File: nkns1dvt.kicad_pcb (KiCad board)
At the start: 2 copper layers, 168.9 x 126.5 mm, 79 parts, among them J1 MJ-4PP-9, J2 SERIAL_LED, SW1 SW_RESET, SW10 SW_PUSH, SW11 SW_PUSH, SW12 SW_PUSH, SW13 SW_PUSH, SW14 SW_PUSH, SW15 SW_PUSH, SW16 SW_PUSH, SW17 SW_PUSH, SW18 SW_PUSH, SW19 SW_PUSH, SW2 SW_PUSH, SW20 SW_PUSH, SW21 SW_PUSH, SW22 SW_PUSH, SW23 SW_PUSH, SW24 SW_PUSH, SW25 SW_PUSH, SW26 SW_PUSH, SW27 SW_PUSH, SW28 SW_PUSH, SW29 SW_PUSH, SW3 SW_PUSH, SW30 SW_PUSH, SW31 SW_PUSH, SW32 SW_PUSH, SW33 SW_PUSH, SW34 SW_PUSH, SW4 SW_PUSH, SW5 SW_PUSH, SW6 SW_PUSH, SW7 SW_PUSH, SW8 SW_PUSH, SW9 SW_PUSH, U1 ProMicro

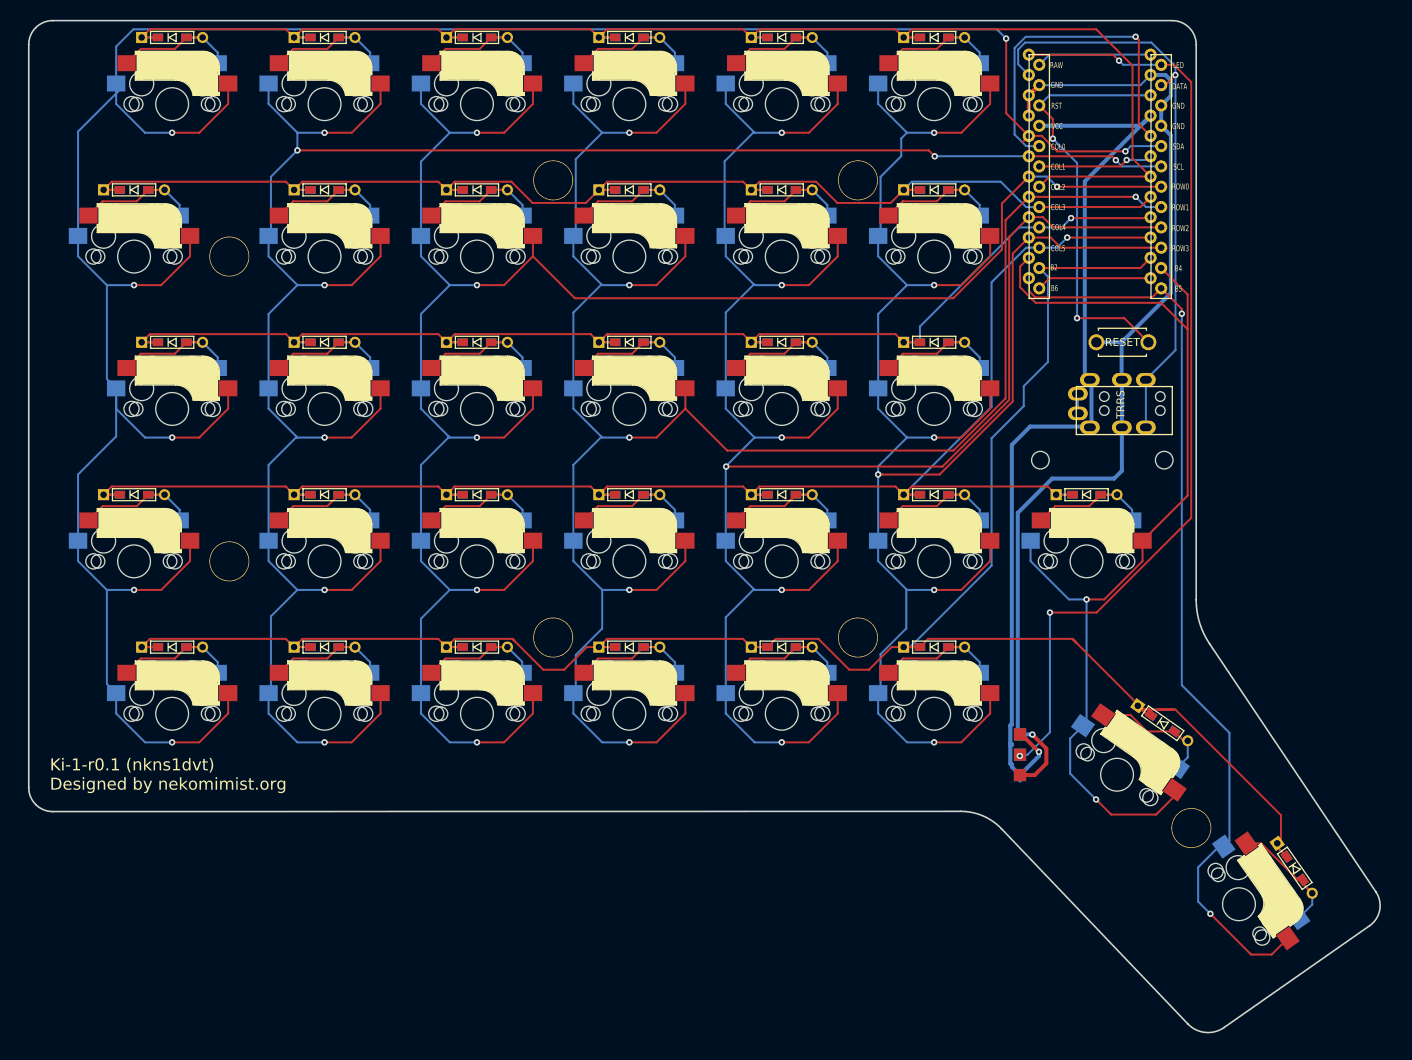
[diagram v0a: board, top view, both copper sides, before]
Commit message: Pro Micro横の基板幅を2mmほど小さくした
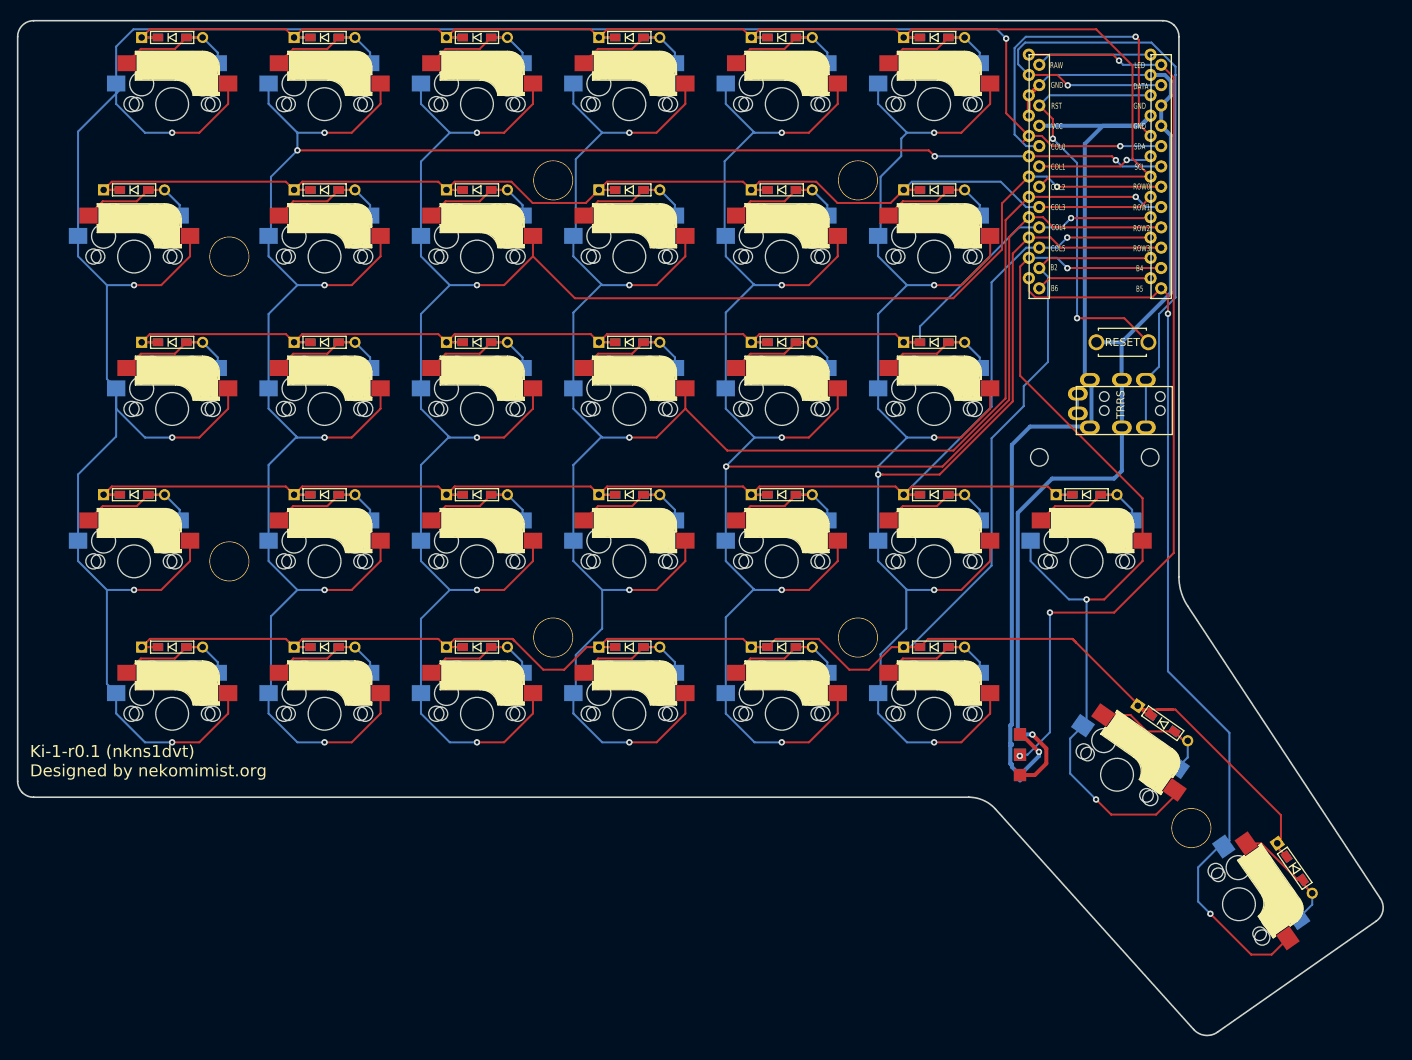
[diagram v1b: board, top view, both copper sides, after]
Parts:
- moved Hole2 1.79 mm to (168.5, 75.8)
- moved Hole1 0.37 mm to (154.7, 75.8)
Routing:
- net data: track 73.9 -> 88.7 mm
- net col6: track 127.6 -> 121.8 mm, vias 2 -> 3
- net VCC: track 119.0 -> 121.8 mm
- net led: track 120.5 -> 119.0 mm
- net col0: track 329.3 -> 328.7 mm
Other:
- board size 168.9 x 126.5 mm -> 170.7 x 126.8 mm

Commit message: Fix
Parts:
- Hole M1: renamed from Hole1; value Hole M2 -> (none)
- Hole M2: renamed from Hole2; value Hole M2 -> (none)
- moved Hole4 9.82 mm to (55.8, 98.4)
- moved Hole1 9.81 mm to (55.8, 41.2)
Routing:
- net col4: track 248.0 -> 245.6 mm
- net col5: track 227.0 -> 224.8 mm
- net GND: track 131.7 -> 129.7 mm
- net row1: track 164.5 -> 166.4 mm
- net col1: track 276.9 -> 278.4 mm, vias 8 -> 7
- net row4: track 268.6 -> 270.1 mm
- net col0: track 328.7 -> 327.6 mm
- net col3: track 256.9 -> 256.2 mm
- net col2: track 259.4 -> 258.8 mm
- net VCC: track 121.8 -> 121.2 mm
- added copper zone on B.Cu, net GND
- added copper zone on F.Cu, net GND
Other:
- board text added: "GND"
- board text added: "LED"
- board text added: "VCC"
